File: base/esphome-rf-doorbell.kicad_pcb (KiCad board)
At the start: 2 copper layers, 65 x 54.7 mm, 70 parts, among them J1 B4B-XH, J2 CONUFL001-SMD-T, J3 Conn_01x01, J4 Conn_01x01, SW1 Boot, U1 MP5493GJ-Z, U2 RFM69W, U3 G3VM-31DR, U4 ESP32-S2-MINI-2, U5 G3VM-63ER, U6 TLP2391

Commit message: New board rev, frist draft of ESPHome component
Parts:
- removed the C7 at (112.2, 80.6)
- removed the C8 at (124.8, 78.2)
- removed the REF** at (149.3, 112.2)
- removed the REF** at (122.5, 113.8)
- removed the REF** at (131.5, 112.4)
- removed the REF** at (122.0, 72.1)
- removed the REF** at (118.6, 86.2)
- removed the TP7 at (133.1, 88.0)
- added BT1: ~, Connector_Molex:Molex_PicoBlade_53261-0271_1x02-1MP_P1.25mm_Horizontal, F.Cu at (114.2, 88.4)
- added C10: 10uF 10V, Capacitor_SMD:C_0603_1608Metric, F.Cu at (124.2, 79.3)
- added C11: 1uF, Capacitor_SMD:C_0402_1005Metric, F.Cu at (139.3, 118.8)
- added C12: 1uF, Capacitor_SMD:C_0402_1005Metric, F.Cu at (142.5, 118.8)
- added C13: 0.1uF, Capacitor_SMD:C_0402_1005Metric, F.Cu at (116.7, 99.7)
- added C14: 22uF 6.3V, Capacitor_SMD:C_0603_1608Metric, F.Cu at (139.9, 99.2)
- added C15: 4.7uF, Capacitor_SMD:C_0603_1608Metric, F.Cu at (139.4, 93.9)
- added C16: 47nF, Capacitor_SMD:C_0402_1005Metric, F.Cu at (111.3, 99.6)
- added C23: 1uF 50V, Capacitor_SMD:C_0805_2012Metric, F.Cu at (161.4, 76.8)
- added C5: 0.1uF 25V, Capacitor_SMD:C_0402_1005Metric, F.Cu at (130.3, 80.2)
- added C6: 4.7uF, Capacitor_SMD:C_0603_1608Metric, F.Cu at (128.5, 75.9)
- added C9: 330nF, Capacitor_SMD:C_0402_1005Metric, F.Cu at (120.8, 73.3)
- added D4: Green, LED_SMD:LED_0603_1608Metric, F.Cu at (114.8, 78.2)
- added FID1: Fiducial, Fiducial:Fiducial_0.5mm_Mask1mm, F.Cu at (110.3, 68.2)
- added FID2: Fiducial, Fiducial:Fiducial_0.5mm_Mask1mm, F.Cu at (170.8, 68.1)
- added FID3: Fiducial, Fiducial:Fiducial_0.5mm_Mask1mm, F.Cu at (112.1, 119.6)
- added JP1: SolderJumper_2_Open, Jumper:SolderJumper-2_P1.3mm_Open_RoundedPad1.0x1.5mm, F.Cu at (118.2, 80.8)
- added JP2: SolderJumper_2_Open, Jumper:SolderJumper-2_P1.3mm_Open_RoundedPad1.0x1.5mm, F.Cu at (118.2, 78.2)
- added R10: 0, Resistor_SMD:R_0402_1005Metric, F.Cu at (137.3, 96.1)
- added R12: 25m, Resistor_SMD:R_Shunt_Vishay_WSK2512_6332Metric_T1.19mm, F.Cu at (114.1, 96.6)
- added R13: 4.7k, Resistor_SMD:R_0402_1005Metric, F.Cu at (113.0, 104.8)
- added R14: 4.7k, Resistor_SMD:R_1206_3216Metric, F.Cu at (113.0, 103.2)
- added R18: 4.7k, Resistor_SMD:R_1206_3216Metric, F.Cu at (129.7, 103.0)
- added R19: 4.7k, Resistor_SMD:R_0402_1005Metric, F.Cu at (130.5, 101.0)
- added R7: 10k, Resistor_SMD:R_0603_1608Metric, F.Cu at (125.1, 104.2)
- added R9: 619k, Resistor_SMD:R_0603_1608Metric, F.Cu at (138.3, 99.2)
- added REF**: KiCad-Logo2_5mm_SilkScreen, Symbol:KiCad-Logo2_5mm_SilkScreen, B.Cu at (117.4, 72.1)
- added REF**: OSHW-Logo2_7.3x6mm_SilkScreen, Symbol:OSHW-Logo2_7.3x6mm_SilkScreen, B.Cu at (128.3, 72.3)
- added RV1: 10k, Potentiometer_SMD:Potentiometer_Bourns_TC33X_Vertical, F.Cu at (116.0, 72.9)
- added RV2: 5k 0.25W, Potentiometer_SMD:Potentiometer_Bourns_3214W_Vertical, F.Cu at (156.8, 78.3)
- added TH1: 10k, Resistor_THT:R_Axial_DIN0204_L3.6mm_D1.6mm_P5.08mm_Vertical, B.Cu at (121.4, 95.8)
- added TP1: TestPoint, TestPoint:TestPoint_Pad_D1.5mm, F.Cu at (122.6, 72.9)
- added TP11: TestPoint, TestPoint:TestPoint_Pad_D1.5mm, F.Cu at (160.8, 79.1)
- added TP4: TestPoint, TestPoint:TestPoint_Pad_D1.5mm, F.Cu at (123.2, 86.9)
- added TP5: TestPoint, TestPoint:TestPoint_Pad_D1.5mm, F.Cu at (111.1, 72.9)
- added U3: TPS7A2033, Package_SON:Texas_X2SON-4_1x1mm_P0.65mm, F.Cu at (140.9, 119.1)
- added U4: MAX17261xxTD, Package_DFN_QFN:TDFN-14-1EP_3x3mm_P0.4mm_EP1.78x2.35mm, F.Cu at (114.0, 100.3)
- added U5: TPS629206DRLR, lib:SOT5X3-8_DRL_TEX, F.Cu at (139.2, 96.2)
- C1: value 10uF -> 1uF; footprint Capacitor_SMD:C_0805_2012Metric -> Capacitor_SMD:C_0402_1005Metric
- C2: value 0.1uF -> 47nF; moved to B.Cu
- C3: value 15pF -> 22uF 16V; footprint Resistor_SMD:R_0402_1005Metric -> Capacitor_SMD:C_0805_2012Metric
- C4: value 10uF -> 10uF 25V
- D1: value 2A -> PMEG2005EJ-QX; footprint Diode_SMD:D_SMA -> Diode_SMD:D_SOD-323F
- D2: value P4SMAJ24CA-AQ -> SMBJ15CA; footprint Diode_SMD:D_SMA -> Diode_SMD:D_SMB
- D3: value 2A -> Red; footprint Diode_SMD:D_SMA -> LED_SMD:LED_0603_1608Metric
- F1: value 1A -> 250mA; footprint Fuse:Fuse_0603_1608Metric -> Fuse:Fuse_1206_3216Metric
- L1: value 15uH -> 1.5uH; footprint Inductor_SMD:L_APV_ANR8040 -> Inductor_SMD:L_Wuerth_MAPI-4020
- L2: value 4.7uH -> 2.2uH; footprint Inductor_SMD:L_Coilcraft_XAL6060-XXX -> Inductor_SMD:L_1210_3225Metric
- R1: value 88.6k -> 1k
- R11: value 1.8k 200mW -> 137k
- R17: renamed from R10; footprint Resistor_SMD:R_0402_1005Metric_Pad0.72x0.64mm_HandSolder -> Resistor_SMD:R_0402_1005Metric
- R2: value 43k -> 1k
- R24: renamed from R15; footprint Resistor_SMD:R_0402_1005Metric_Pad0.72x0.64mm_HandSolder -> Resistor_SMD:R_0402_1005Metric
- R3: value 10k -> 1.2k
- R4: value 13.7k -> 5.23k; footprint Resistor_SMD:R_0603_1608Metric -> Resistor_SMD:R_0402_1005Metric
- R5: value 40.2k -> 4.99k
- R6: value 33.2k -> 30.1k; footprint Resistor_SMD:R_0603_1608Metric -> Resistor_SMD:R_0402_1005Metric
- U1: value MP5493GJ-Z -> BQ25628E; footprint lib:SOT65P280X100-8N -> lib:WQFN-HR18__RYK_TEX
- moved L2 34.1 mm to (142.2, 97.0), turned to -90 degrees
- moved R1 27.1 mm to (111.4, 80.8), turned to 0 degrees
- moved R11 26.7 mm to (136.8, 99.2)
- moved R3 22.4 mm to (119.4, 72.9), turned to -90 degrees
- moved R2 20.7 mm to (111.4, 78.2)
- moved R5 19.0 mm to (113.0, 72.7), turned to -90 degrees
- moved C4 18.2 mm to (131.6, 80.6), turned to -90 degrees
- moved D3 16.6 mm to (114.9, 80.8), turned to 180 degrees
- moved TP6 14.5 mm to (142.6, 79.3)
- moved R6 12.7 mm to (123.1, 94.1), turned to 0 degrees
- moved L1 12.1 mm to (128.1, 86.8), turned to 180 degrees
- moved REF** 11.9 mm to (139.5, 109.5)
- moved TP7 10.7 mm to (141.8, 85.6)
- moved D1 10.0 mm to (148.9, 74.7), turned to 90 degrees
- moved TP10 10.0 mm to (167.3, 91.9)
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- renumbered C9 to C17, C10 to C18, C11 to C19, C12 to C20, C14 to C21, C13 to C22, C5 to C7, C6 to C8, D4 to D5, D5 to D7, JP1 to JP3, JP3 to JP4, JP2 to JP5, R8 to R15, R9 to R16, R16 to R20, R13 to R21, R12 to R22, R14 to R23, R7 to R8, TP6 to TP10, TP1 to TP6, TP3 to TP7, TP4 to TP8, TP5 to TP9, U3 to U6, U4 to U7, U5 to U8, U6 to U9
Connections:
- C19 pad 1: +3.3V -> +3.3VP
- C2 pad 1: /VIN -> /SW
- C2 pad 2: GND -> /BTST
- C20 pad 1: +3.3V -> +3.3VP
- C21 pad 1: +3.3V -> +3.3VP
- C3 pad 1: +3.3V -> VBUS
- C3 pad 2: /FB1 -> GND
- C4 pad 1: +3.3V -> Net-(U1-PMID)
- C7 pad 1: +3.3V -> +3.3VA
- C8 pad 1: +3.3V -> +3.3VA
- D3 pad 1: /VIN -> Net-(D3-K)
- D3 pad 2: /SW2 -> Net-(D3-A)
- JP4 pad 2: +3.3V -> +3.3VP
- L1 pad 1: /SW1 -> /SW
- L1 pad 2: +3.3V -> VBUS
- L2 pad 1: Net-(C7-Pad1) -> Net-(U5-SW)
- L2 pad 2: /SW2 -> +3.3VP
- R1 pad 1: Net-(D1-A) -> VBUS
- R1 pad 2: /VBS -> Net-(D3-A)
- R11 pad 1: GND -> Net-(U5-FB/VSET)
- R11 pad 2: Net-(U6-A) -> GND
- R2 pad 1: +3.3V -> VBUS
- R2 pad 2: /FB1 -> Net-(D4-A)
- R22 pad 1: +3.3V -> +3.3VP
- R3 pad 1: /VBS -> GND
- R3 pad 2: GND -> Net-(U1-ILIM)
- R4 pad 1: /FB1 -> /TH
- R4 pad 2: GND -> Net-(U1-TS_BIAS)
- R5 pad 1: Net-(C7-Pad1) -> GND
- R5 pad 2: /FB2 -> Net-(R5-Pad2)
- R6 pad 1: /FB2 -> GND
- R6 pad 2: GND -> /TH
- R8 pad 1: +3.3V -> +3.3VP
- TP2 pad 1: +3.3V -> +3.3VP
- U1 pad 1: /FB1 -> /BTST
- U1 pad 2: /~{POWER_FAIL} -> Net-(U1-REGN)
- U1 pad 3: /SW1 -> Net-(JP2-A)
- U1 pad 4: /VBS -> Net-(U1-ILIM)
- U1 pad 5: GND -> Net-(U1-TS_BIAS)
- U1 pad 6: /SW2 -> /TH
- U1 pad 7: /VIN -> unconnected-(U1-~{QON}-Pad7)
- U1 pad 8: /FB2 -> +BATT
- U2 pad 8: +3.3V -> +3.3VA
- U7 pad 19: /~{POWER_FAIL} -> /SCL1
- U7 pad 20: unconnected-(U4-IO16-Pad20) -> /SDA1
- U7 pad 21: unconnected-(U4-IO17-Pad21) -> /~{INT}
- U7 pad 22: unconnected-(U4-IO18-Pad22) -> /~{CE}
- U7 pad 25: unconnected-(U4-IO21-Pad25) -> /RF_PWR_EN
- U7 pad 3: +3.3V -> +3.3VP
- U7 pad 31: unconnected-(U4-IO35-Pad31) -> /SCL2
- U7 pad 32: unconnected-(U4-IO36-Pad32) -> /SDA2
- U7 pad 33: unconnected-(U4-IO37-Pad33) -> /BAT_ALERT
- U9 pad 1: Net-(U6-A) -> GND
- U9 pad 3: /S_IN -> Net-(U9-K)
- U9 pad 6: +3.3V -> +3.3VP
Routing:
- net +3.3VP: track 0.00 -> 118.3 mm, vias 0 -> 10
- net +3.3V: track 110.2 -> 0.00 mm, vias 6 -> 0
- net VBUS: track 0.00 -> 67.7 mm, vias 0 -> 5
- net /SW2: track 52.3 -> 0.00 mm
- net /TH: track 0.00 -> 39.3 mm, vias 0 -> 4
- net /~{CE}: track 0.00 -> 36.2 mm, vias 0 -> 2
- net /~{INT}: track 0.00 -> 33.5 mm
- net /SDA1: track 0.00 -> 33.3 mm
- net /SCL1: track 0.00 -> 33.1 mm
- net +BATT: track 0.00 -> 32.7 mm, vias 0 -> 2
- net Net-(U1-TS_BIAS): track 0.00 -> 26.9 mm, vias 0 -> 2
- net /RF_PWR_EN: track 0.00 -> 25.2 mm, vias 0 -> 2
- net /~{POWER_FAIL}: track 23.1 -> 0.00 mm, vias 2 -> 0
- net /VIN: track 3.22 -> 20.5 mm
- net Net-(C7-Pad1): track 15.4 -> 0.00 mm
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- added copper zone on F.Cu, net +BATT
- added copper zone on F.Cu, net /BTST
- added copper zone on F.Cu, net /SW
- added copper zone on F.Cu, net Net-(U4-CSPL)
- added copper zone on F.Cu, net Net-(U5-SW)
- added copper zone on F.Cu, net VBUS
- removed copper zone on F.Cu, net /SW1
- removed copper zone on F.Cu, net /SW2
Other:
- outline, holes or cut-outs redrawn
- board text added: "+3.3V (ESP)"
- board text added: "100mA"
- board text added: "15kΩ"
- board text added: "33.3mA"
- board text added: "4.99kΩ"
- board text added: "BOOT"
- board text added: "I_{CHG}"
- board text added: "PG"
- board text added: "RX"
- board text added: "R_{ISET}"
- board text added: "STAT"
- board text removed: "+"
- board text removed: "+3.3V"
- board text removed: "-"
- board text removed: "UX"
- board text removed: "~{PFAIL}"

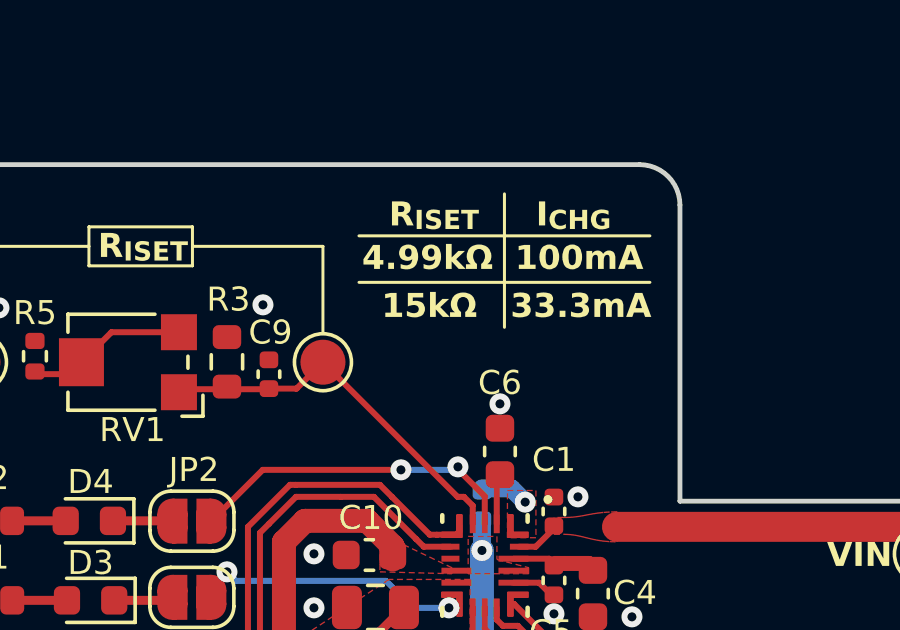
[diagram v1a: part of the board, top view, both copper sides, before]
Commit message: Fix read_register_word_ call - use reference not pointer
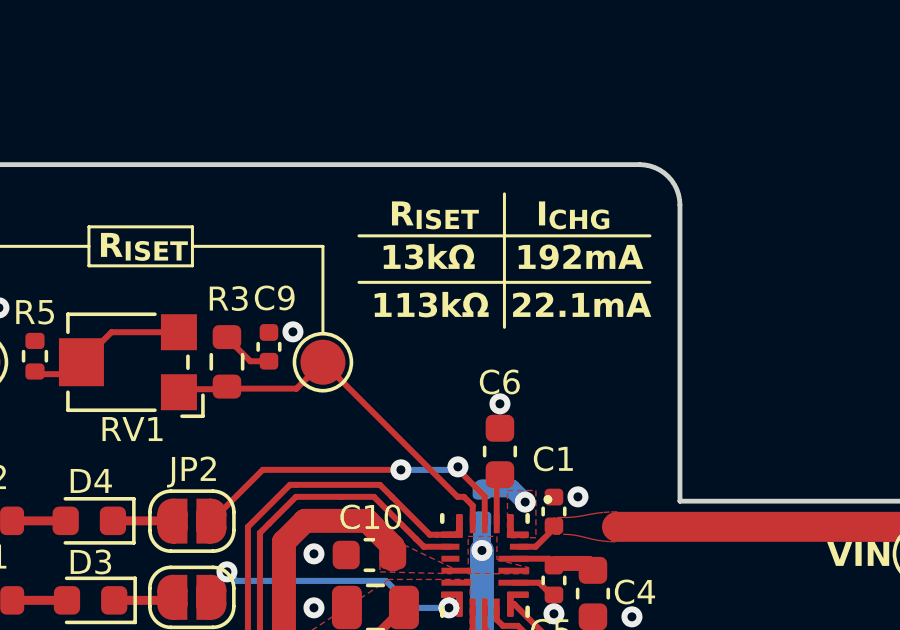
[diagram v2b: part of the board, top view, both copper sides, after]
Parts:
- R5: value 4.99k -> 13k
- RV1: value 10k -> 100k
- moved C9 0.91 mm to (120.8, 72.4)
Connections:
- C9 pad 2: Net-(U1-ILIM) -> Net-(C9-Pad2)
- R3 pad 1: GND -> Net-(C9-Pad2)
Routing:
- net Net-(C9-Pad2): track 0.00 -> 1.75 mm
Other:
- board text added: "113kΩ"
- board text added: "13kΩ"
- board text added: "192mA"
- board text added: "22.1mA"
- board text removed: "100mA"
- board text removed: "15kΩ"
- board text removed: "33.3mA"
- board text removed: "4.99kΩ"

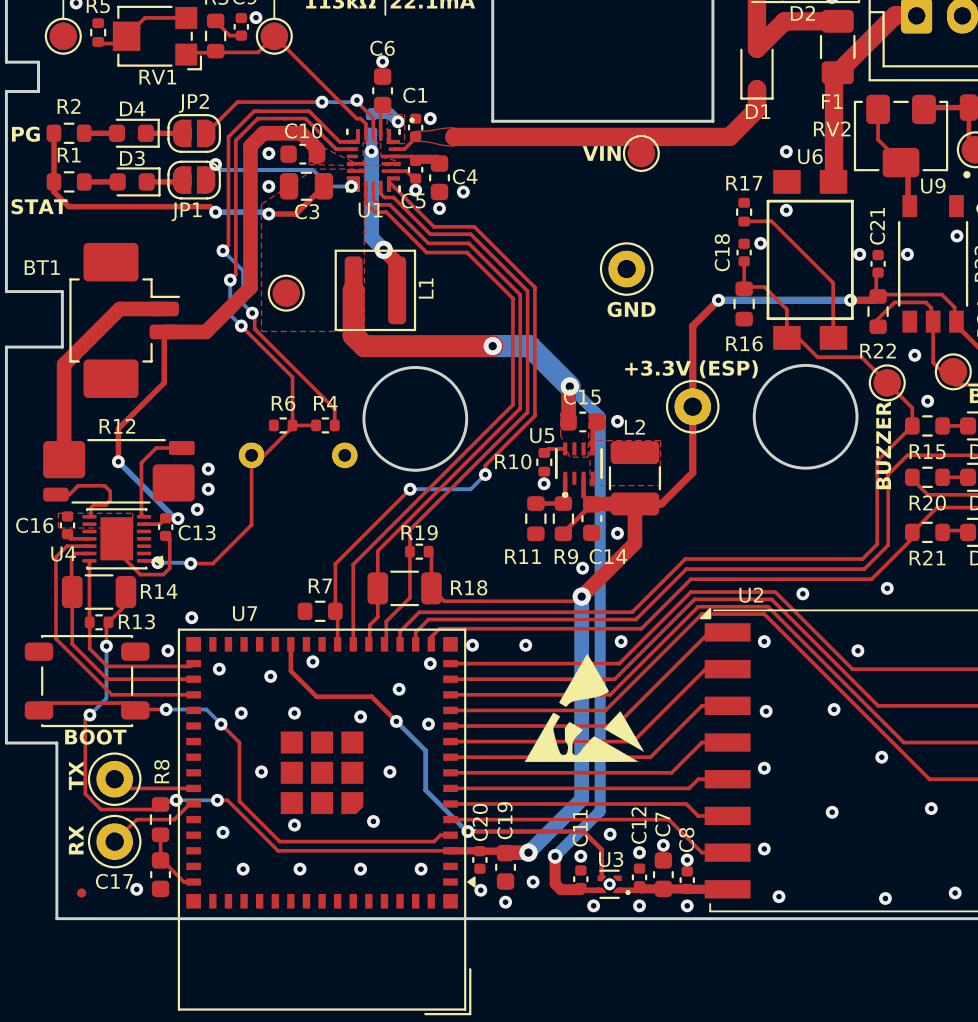
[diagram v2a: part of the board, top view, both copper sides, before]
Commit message: Update interrupt pin mapping
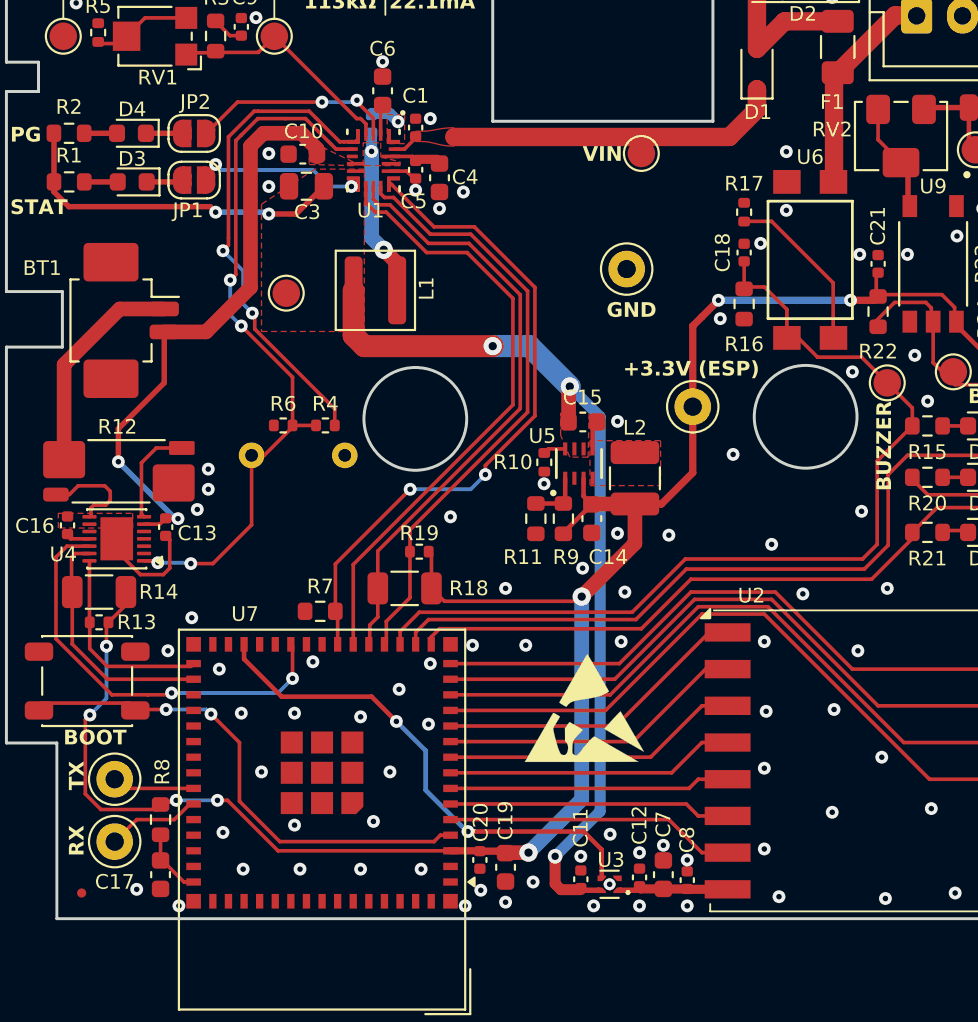
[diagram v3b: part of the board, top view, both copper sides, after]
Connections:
- U7 pad 25: /RF_PWR_EN -> /BAT_ALERT
- U7 pad 28: unconnected-(U7-IO33-Pad28) -> /RF_PWR_EN
- U7 pad 33: /BAT_ALERT -> unconnected-(U7-IO37-Pad33)
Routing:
- net /BAT_ALERT: track 15.3 -> 22.9 mm, vias 0 -> 2
- net /RF_PWR_EN: track 25.2 -> 27.4 mm
- net GND: vias 91 -> 101

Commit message: Fix paths
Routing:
- net GND: vias 101 -> 125
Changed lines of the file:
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@@
 		)
 		(embedded_fonts no)
-		(model "/home/q425942/private/projects/esphome-rf-doorbell/lib/TLP2391_TPL_E.step"
+		(model "${KIPRJMOD}/../lib/TLP2391_TPL_E.step"
 			(offset
 				(xyz 0 0 0)
@@
 		)
 		(embedded_fonts no)
-		(model "/home/q425942/private/projects/esphome-rf-doorbell/lib/G3VM-21DR--3DModel-STEP-1.STEP"
+		(model "${KIPRJMOD}/../lib/G3VM-21DR--3DModel-STEP-1.STEP"
 			(offset
 				(xyz -1.25 0.05 0)
@@
 	)
 	(via
+		(at 109.4 90.9)
+		(size 0.7)
+		(drill 0.3)
+		(layers "F.Cu" "B.Cu")
+		(free yes)
+		(net 1)
+	)
+	(via
 		(at 141.5 105.9)
 		(size 0.7)
@@
 	)
 	(via
+		(at 123.8 99.8)
+		(size 0.7)
+		(drill 0.3)
+		(layers "F.Cu" "B.Cu")
+		(free yes)
+		(net 1)
+	)
+	(via
 		(at 157.5 90.3)
 		(size 0.7)
@@
 	)
 	(via
+		(at 136 84.6)
+		(size 0.7)
+		(drill 0.3)
+		(layers "F.Cu" "B.Cu")
+		(free yes)
+		(net 1)
+	)
+	(via
 		(at 127.3 110)
 		(size 0.7)
@@
 	)
 	(via
+		(at 147.5 71.9)
+		(size 0.7)
+		(drill 0.3)
+		(layers "F.Cu" "B.Cu")
+		(free yes)
+		(net 1)
+	)
+	(via
 		(at 131.1 77.4)
 		(size 0.7)
@@
 	)
 	(via
+		(at 114.1 67.3)
+		(size 0.7)
+		(drill 0.3)
+		(layers "F.Cu" "B.Cu")
+		(free yes)
+		(net 1)
+	)
+	(via
+		(at 116.9 93.9)
+		(size 0.7)
+		(drill 0.3)
+		(layers "F.Cu" "B.Cu")
+		(free yes)
+		(net 1)
+	)
+	(via
+		(at 168 67.7)
+		(size 0.7)
+		(drill 0.3)
+		(layers "F.Cu" "B.Cu")
+		(free yes)
+		(net 1)
+	)
+	(via
+		(at 172 97.5)
+		(size 0.7)
+		(drill 0.3)
+		(layers "F.Cu" "B.Cu")
+		(free yes)
+		(net 1)
+	)
+	(via
+		(at 167.1 99.5)
+		(size 0.7)
+		(drill 0.3)
+		(layers "F.Cu" "B.Cu")
+		(free yes)
+		(net 1)
+	)
+	(via
 		(at 119.8 116.3)
 		(size 0.7)
@@
 	)
 	(via
+		(at 164.2 86.1)
+		(size 0.7)
+		(drill 0.3)
+		(layers "F.Cu" "B.Cu")
+		(free yes)
+		(net 1)
+	)
+	(via
 		(at 136.3 106.1)
 		(size 0.7)
@@
 	)
 	(via
+		(at 125.4 74.1)
+		(size 0.7)
+		(drill 0.3)
+		(layers "F.Cu" "B.Cu")
+		(free yes)
+		(net 1)
+	)
+	(via
+		(at 147.4 76.4)
+		(size 0.7)
+		(drill 0.3)
+		(layers "F.Cu" "B.Cu")
+		(free yes)
+		(net 1)
+	)
+	(via
 		(at 122.3 81.1)
 		(size 0.7)
@@
 	)
 	(via
+		(at 118.9 90.4)
+		(size 0.7)
+		(drill 0.3)
+		(layers "F.Cu" "B.Cu")
+		(free yes)
+		(net 1)
+	)
+	(via
 		(at 169.6 110.6)
 		(size 0.7)
@@
 	)
 	(via
+		(at 171.8 77.1)
+		(size 0.7)
+		(drill 0.3)
+		(layers "F.Cu" "B.Cu")
+		(free yes)
+		(net 1)
+	)
+	(via
 		(at 158.4 115)
 		(size 0.7)
@@
 	)
 	(via
+		(at 112.3 93.7)
+		(size 0.7)
+		(drill 0.3)
+		(layers "F.Cu" "B.Cu")
+		(free yes)
+		(net 1)
+	)
+	(via
 		(at 119 97.6)
 		(size 0.7)
@@
 	)
 	(via
+		(at 117.4 83.9)
+		(size 0.7)
+		(drill 0.3)
+		(layers "F.Cu" "B.Cu")
+		(free yes)
+		(net 1)
+	)
+	(via
+		(at 108.8 102.7)
+		(size 0.7)
+		(drill 0.3)
+		(layers "F.Cu" "B.Cu")
+		(free yes)
+		(net 1)
+	)
+	(via
 		(at 123.7 109.8)
 		(size 0.7)
@@
 	)
 	(via
+		(at 171 72.5)
+		(size 0.7)
+		(drill 0.3)
+		(layers "F.Cu" "B.Cu")
+		(free yes)
+		(net 1)
+	)
+	(via
 		(at 170.88 104.3)
 		(size 0.7)
@@
 	)
 	(via
+		(at 123.7 75.6)
+		(size 0.7)
+		(drill 0.3)
+		(layers "F.Cu" "B.Cu")
+		(free yes)
+		(net 1)
+	)
+	(via
 		(at 133.4 106.1)
 		(size 0.7)
@@
 	)
 	(via
+		(at 133.4 74.1)
+		(size 0.7)
+		(drill 0.3)
+		(layers "F.Cu" "B.Cu")
+		(free yes)
+		(net 1)
+	)
+	(via
 		(at 117.4 120.3)
 		(size 0.7)
@@
 	)
 	(via
+		(at 109.5 83.8)
+		(size 0.7)
+		(drill 0.3)
+		(layers "F.Cu" "B.Cu")
+		(free yes)
+		(net 1)
+	)
+	(via
 		(at 128.5 74.3)
 		(size 0.7)
@@
 	)
 	(via
+		(at 171.9 85.6)
+		(size 0.7)
+		(drill 0.3)
+		(layers "F.Cu" "B.Cu")
+		(free yes)
+		(net 1)
+	)
+	(via
 		(at 139.3 117.6)
 		(size 0.7)
@@
 	)
 	(via
+		(at 135 79.6)
+		(size 0.7)
+		(drill 0.3)
+		(layers "F.Cu" "B.Cu")
+		(free yes)
+		(net 1)
+	)
+	(via
 		(at 116.8 106.4)
 		(size 0.7)
@@
 		(size 0.7)
 		(drill 0.3)
+		(layers "F.Cu" "B.Cu")
+		(free yes)
+		(net 1)
+	)
+	(via
+		(at 109 70.3)
+		(size 0.7)
+		(drill 0.3)
